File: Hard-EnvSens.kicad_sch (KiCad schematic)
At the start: 96 parts, among them J1 TYPE-C-31-M-12, J2 Conn_01x04_Socket, J3 Conn_02x02_Odd_Even, J4 Conn_01x04_Pin, J5 Conn_02x02_Odd_Even, J6 Conn_01x02_Pin, J7 Conn_01x04_Pin, Q1 SS8050, Q2 SS8050, SW1 SW_Push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

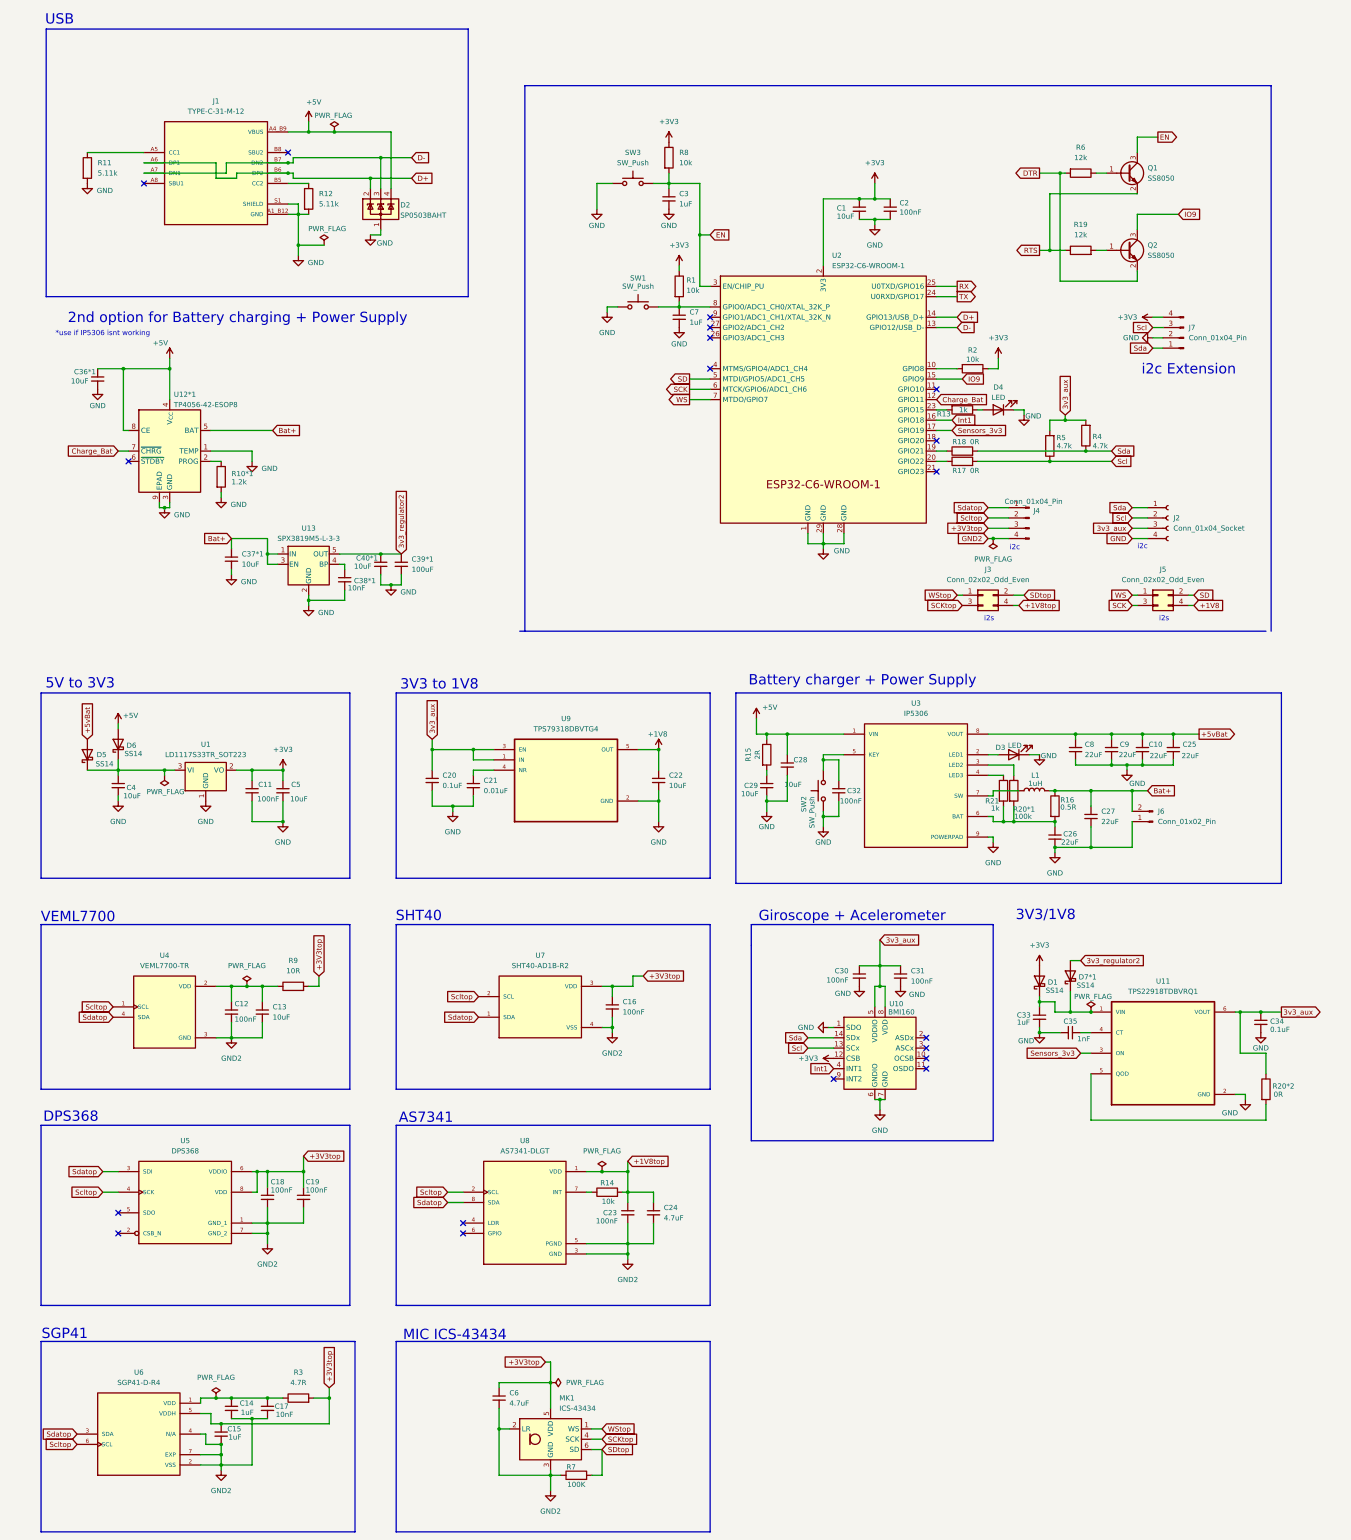
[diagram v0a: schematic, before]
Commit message: Almost finished board
New 3v3 regulaator
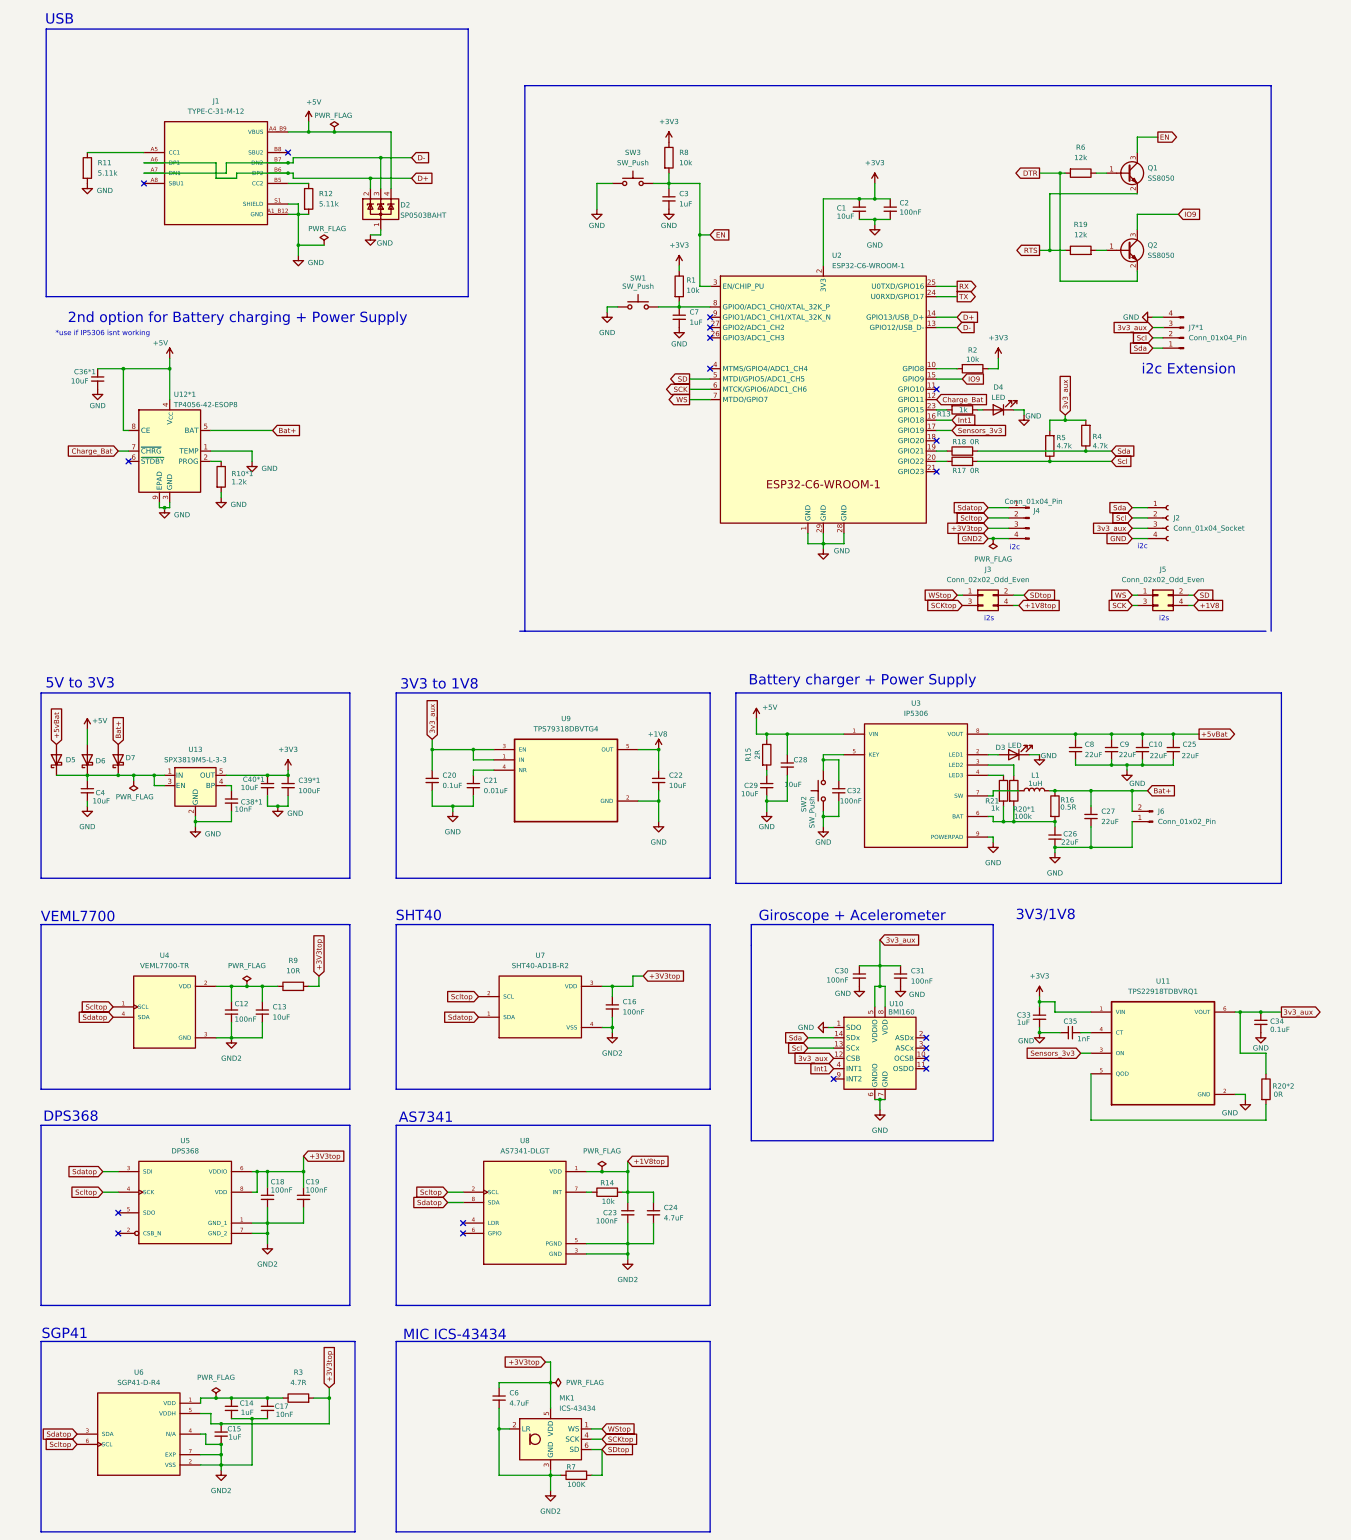
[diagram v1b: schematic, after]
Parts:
- removed C11: 100nF, Capacitor_SMD:C_0603_1608Metric, symbol Device:C_Small
- removed C37*1, C5: 10uF, Capacitor_SMD:C_0603_1608Metric, symbol Device:C_Small
- removed D1, D7*1: SS14, Diode_SMD:D_SMA, symbol Diode:SS14
- removed U1: LD1117S33TR_SOT223, Package_TO_SOT_SMD:SOT-223-3_TabPin2, symbol Regulator_Linear:LD1117S33TR_SOT223
- added D7: CMS30I30A, Diode_SMD:D_SMA, symbol Diode:SS14
- D5, D6: value SS14 -> CMS30I30A
- U11: footprint TPS22918TDBVRQ1:SOT95P280X145-6N -> libs:SOT95P280X145-6N
- renumbered J7 to J7*1
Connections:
- net 3v3_regulator2 is gone; now on net +3V3: C39*1.1, C40*1.1, U13.5 (OUT)
- net +3V3: now also C33.1, U11.1 (VIN); no longer J7*1.4 (Pin_4), U10.12 (CSB)
- net 3v3_aux: now also J7*1.3 (Pin_3), U10.12 (CSB)
- net Bat+: now also D7.2 (A); no longer U13.1 (IN), U13.3 (EN)
- net GND: now also J7*1.4 (Pin_4); no longer J7*1.2 (Pin_2)
- net Scl: now also J7*1.2 (Pin_2); no longer J7*1.3 (Pin_3)
- net at C4.1, D5.1 (K), D6.1 (K): now also U13.1 (IN), U13.3 (EN), D7.1 (K)
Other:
- moved on the sheet: C38*1, C39*1, C4, C40*1, D5, D6, U13

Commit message: Almost ready to fabricate
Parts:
- added R32*1: 10k, Resistor_SMD:R_0603_1608Metric, symbol Device:R
- C39: renamed from C39*1; footprint Capacitor_SMD:C_0603_1608Metric -> Capacitor_SMD:C_Elec_6.3x7.7
- C40: renamed from C40*1; value 10uF -> 0.1uF
- R31*1: renamed from R10*1; value 1.2k -> 4k
- renumbered C38*1 to C38, R20*2 to R30*1
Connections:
- net +3V3: now also R32*1.2
- net Charge_Bat: now also R32*1.1
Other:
- moved on the sheet: C33, C34, C35, C39, R30*1, U11

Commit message: ready to fabricate
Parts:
- added 1V8, 3V3, 3V3Sensor1, 5vBoost1, 5vUSB1, Battery1, GND1, RX1, TX1: TestPoint, TestPoint:TestPoint_THTPad_1.5x1.5mm_Drill0.7mm, symbol Connector:TestPoint
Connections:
- net +1V8: now also 1V8.1
- net +3V3: now also 3V3.1
- net +5V: now also 5vUSB1.1
- net +5vBat: now also 5vBoost1.1
- net 3v3_aux: now also 3V3Sensor1.1
- net Bat+: now also Battery1.1
- net GND: now also GND1.1
- net RX: now also RX1.1
- net TX: now also TX1.1
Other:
- moved on the sheet: C22

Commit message: ready to fabricate
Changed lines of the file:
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@@
 	(wire
 		(pts
-			(xy 273.05 63.5) (xy 273.05 77.47)
+			(xy 273.05 64.77) (xy 273.05 77.47)
 		)
 		(stroke
@@
 	(wire
 		(pts
-			(xy 294.64 63.5) (xy 273.05 63.5)
+			(xy 294.64 64.77) (xy 273.05 64.77)
 		)
 		(stroke
@@
 		)
 		(stroke
+			(width 0)
+			(type default)
+		)
+	)
+	(wire
+		(pts
+			(xy 294.64 64.77) (xy 294.64 63.5)
+		)
+		(stroke
